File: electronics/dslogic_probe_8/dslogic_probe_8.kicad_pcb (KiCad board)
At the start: 2 copper layers, 11.3 x 6 mm, 16 parts, among them J1 Conn_02x04_Odd_Even, J2 Conn_02x04_Odd_Even

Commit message: WIP routing and placing
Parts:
- added C5: 100p, SquantorRcl:C_0402, F.Cu at (157.4, 70.9)
- added C6: 100p, SquantorRcl:C_0402, F.Cu at (157.4, 72.0)
- added C7: 100p, SquantorRcl:C_0402, F.Cu at (157.4, 73.1)
- added C8: 100p, SquantorRcl:C_0402, F.Cu at (157.4, 74.2)
- added R10: 100K, SquantorRcl:R_0402_hand, B.Cu at (157.4, 72.0)
- added R11: 100K, SquantorRcl:R_0402_hand, B.Cu at (157.4, 73.1)
- added R12: 100K, SquantorRcl:R_0402_hand, B.Cu at (157.4, 74.2)
- added R13: 470, SquantorRcl:R_0402_hand, F.Cu at (160.0, 70.9)
- added R14: 470, SquantorRcl:R_0402_hand, F.Cu at (160.0, 72.0)
- added R15: 470, SquantorRcl:R_0402_hand, F.Cu at (160.0, 73.1)
- added R16: 470, SquantorRcl:R_0402_hand, F.Cu at (160.0, 74.2)
- added R9: 100K, SquantorRcl:R_0402_hand, B.Cu at (157.4, 70.9)
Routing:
- net Net-(C8-Pad2): track 0.00 -> 2.25 mm, vias 0 -> 1
- net Net-(C7-Pad2): track 0.00 -> 2.25 mm, vias 0 -> 1
- net Net-(C6-Pad2): track 0.00 -> 2.25 mm, vias 0 -> 1
- net Net-(C5-Pad2): track 0.00 -> 2.25 mm, vias 0 -> 1
- net Net-(J2-Pad9): track 0.00 -> 1.50 mm, vias 0 -> 1
- net Net-(J2-Pad15): track 0.00 -> 1.50 mm, vias 0 -> 1
- net Net-(J2-Pad13): track 0.00 -> 1.50 mm, vias 0 -> 1
- net Net-(J2-Pad11): track 0.00 -> 1.50 mm, vias 0 -> 1
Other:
- board size 11.3 x 6 mm -> 11.3 x 10.4 mm

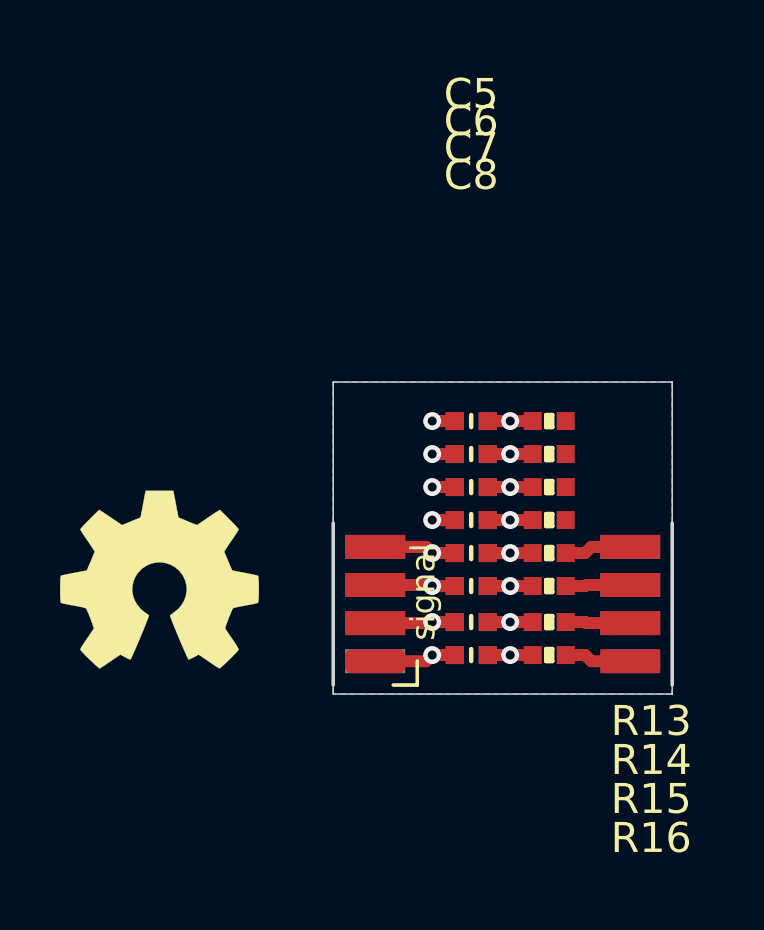
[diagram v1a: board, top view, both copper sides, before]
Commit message: WIP 8 channel dslogic probe
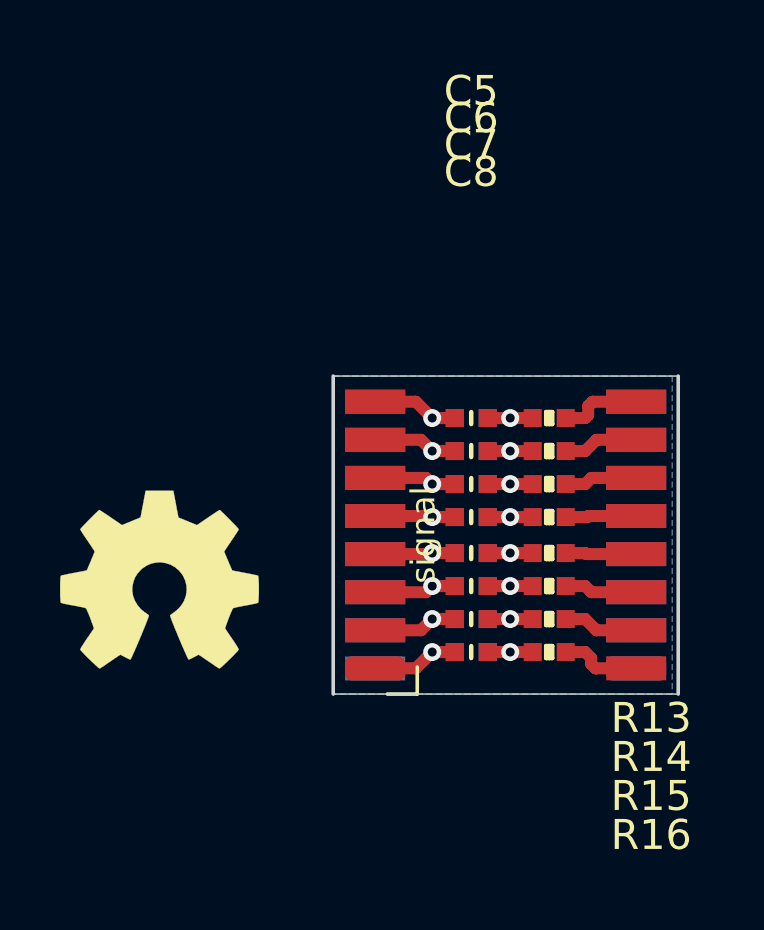
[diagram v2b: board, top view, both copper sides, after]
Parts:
- J1, J2: footprint SquantorConnectors:Header-0127-2X04-EDGE -> SquantorConnectors:Header-0127-2X08-EDGE
- N1: value 20220506 -> 20221004
- moved J1 2.31 mm to (161.8, 74.7)
- moved J2 2.30 mm to (155.3, 74.7)
- moved N1 1.81 mm to (159.8, 74.4)
- moved C4 0.10 mm to (157.4, 78.6)
- moved C5 0.10 mm to (157.4, 70.8)
- moved C8 0.10 mm to (157.4, 74.1)
- moved R12 0.10 mm to (157.4, 74.1)
- moved R13 0.10 mm to (160.0, 70.8)
- moved R16 0.10 mm to (160.0, 74.1)
- moved R4 0.10 mm to (157.4, 78.6)
- moved R8 0.10 mm to (160.0, 78.6)
- moved R9 0.10 mm to (157.4, 70.8)
- moved C3 0.10 mm to (157.4, 77.5)
- moved C6 0.10 mm to (157.4, 71.9)
- moved C7 0.10 mm to (157.4, 73.0)
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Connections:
- C5 pad 1: Net-(J2-Pad15) -> Net-(C5-Pad1)
- C6 pad 1: Net-(J2-Pad13) -> Net-(C6-Pad1)
- C7 pad 1: Net-(J2-Pad11) -> Net-(C7-Pad1)
- C8 pad 1: Net-(J2-Pad9) -> Net-(C8-Pad1)
- R10 pad 1: Net-(J2-Pad13) -> Net-(C6-Pad1)
- R11 pad 1: Net-(J2-Pad11) -> Net-(C7-Pad1)
- R12 pad 1: Net-(J2-Pad9) -> Net-(C8-Pad1)
- R9 pad 1: Net-(J2-Pad15) -> Net-(C5-Pad1)
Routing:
- net Net-(C5-Pad1): track 0.00 -> 3.63 mm, vias 0 -> 1
- net Net-(C6-Pad1): track 0.00 -> 3.56 mm, vias 0 -> 1
- net Net-(C7-Pad1): track 0.00 -> 3.48 mm, vias 0 -> 1
- net Net-(C8-Pad1): track 0.00 -> 3.41 mm, vias 0 -> 1
- net Net-(J1-Pad16): track 0.00 -> 2.75 mm
- net Net-(J1-Pad14): track 0.00 -> 2.51 mm
- net Net-(J1-Pad12): track 0.00 -> 2.43 mm
- net Net-(J1-Pad10): track 0.00 -> 2.36 mm
- net Net-(J2-Pad9): track 1.50 -> 0.00 mm, vias 1 -> 0
- net Net-(J2-Pad15): track 1.50 -> 0.00 mm, vias 1 -> 0
- net Net-(J2-Pad13): track 1.50 -> 0.00 mm, vias 1 -> 0
- net Net-(J2-Pad11): track 1.50 -> 0.00 mm, vias 1 -> 0
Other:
- board size 11.3 x 10.4 mm -> 11.5 x 10.6 mm

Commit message: fixed DRC issues with connectors
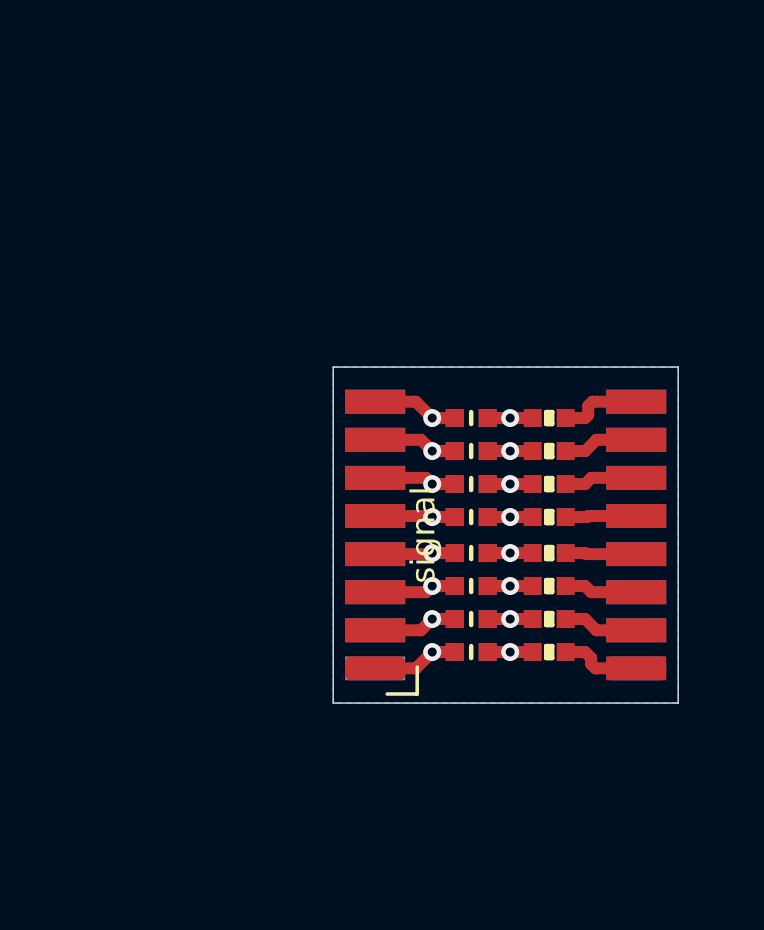
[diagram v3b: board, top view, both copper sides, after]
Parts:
- removed N2: OHWLOGO, Symbol:OSHW-Symbol_6.7x6mm_SilkScreen
- N1: value 20221004 -> 20221007
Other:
- board size 11.5 x 10.6 mm -> 11.5 x 11.2 mm

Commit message: reviewed PCB and updated versionnumber
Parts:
- N1: value 20221007 -> 20221009
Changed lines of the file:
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@@
       (effects (font (size 1 1) (thickness 0.15)) (justify mirror))
     )
-    (fp_text value "20221007" (at 0 0.0875 90) (layer "B.SilkS")
+    (fp_text value "20221009" (at 0 0.0875 90) (layer "B.SilkS")
       (effects (font (size 0.8 0.8) (thickness 0.15)) (justify mirror))
     )
